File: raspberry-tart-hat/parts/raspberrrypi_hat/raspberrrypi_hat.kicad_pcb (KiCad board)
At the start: 4 copper layers, 65 x 56 mm, 18 parts, among them J3 40HAT, J6 CONN_02X02, J9 CONN_01X02, Q1 DMG2305UX, Q2 DMMT5401, U2 CAT24C32

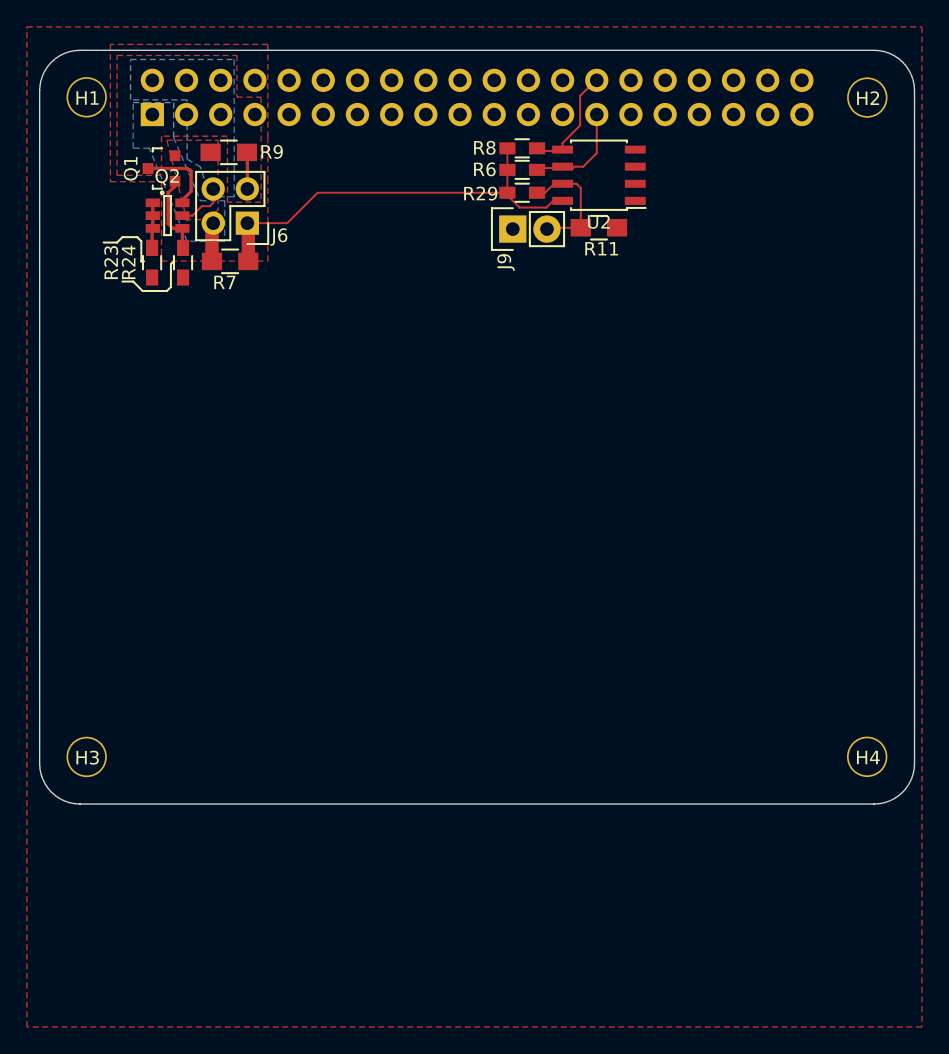
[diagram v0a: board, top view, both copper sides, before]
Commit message: Update imported pi hat project
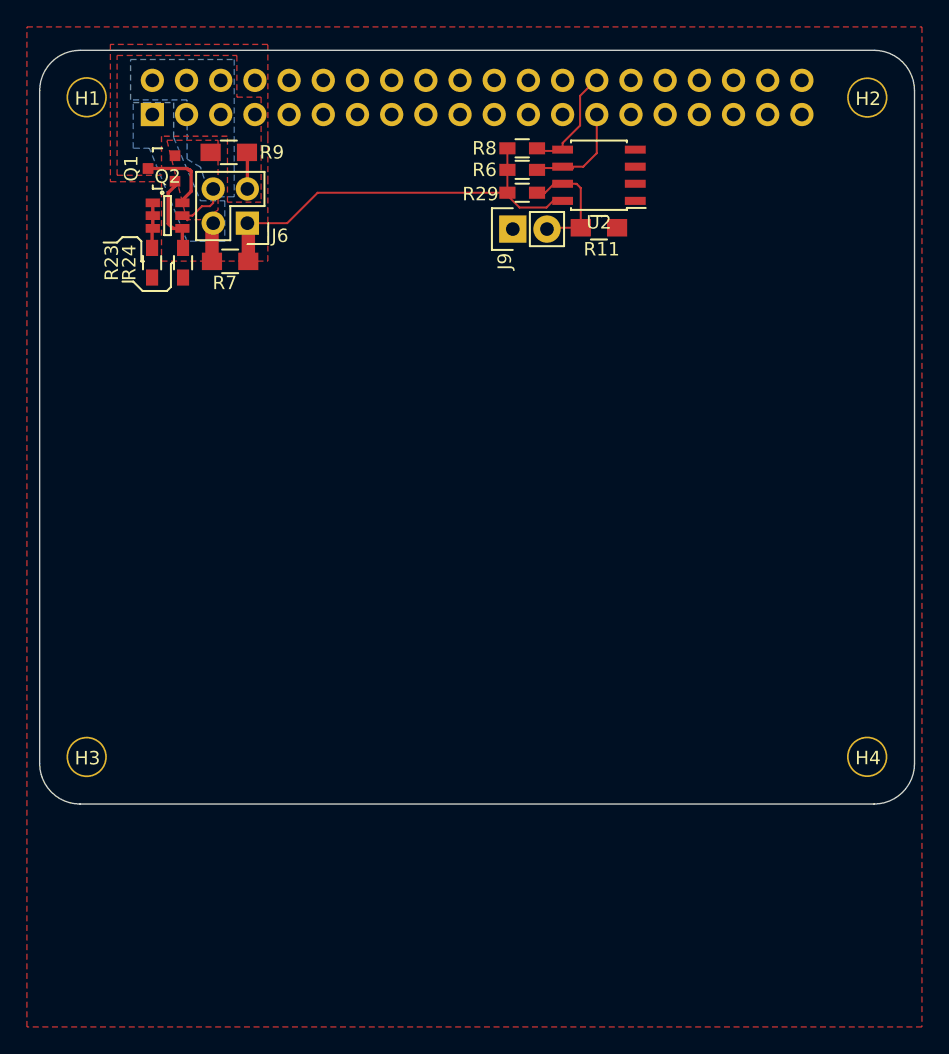
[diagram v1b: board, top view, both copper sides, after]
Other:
- net class Default removed
